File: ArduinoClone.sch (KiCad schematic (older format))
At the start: 0 parts

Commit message: added symboles and child sheet
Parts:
- added BT?: Battery, symbol Device:Battery
- added C? (x2): C, symbol Device:C
- added C?: CP, symbol Device:CP
- added D?: LED, symbol Device:LED
- added R? (x2): R, symbol Device:R
- added U?: 24LC1025, symbol Memory_EEPROM:24LC1025
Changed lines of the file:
@@
 $Descr A4 11693 8268
 encoding utf-8
-Sheet 1 1
-Title "Arduino Clone"
+Sheet 1 2
+Title "Battery powered Arduino clone with clock and extended EEPROM"
 Date "2020-04-18"
 Rev "1"
@@
 Comment4 ""
 $EndDescr
+$Comp
+L Device:Battery BT?
+U 1 1 5E9ADC39
+P 5200 3250
+F 0 "BT?" H 5308 3296 50  0000 L CNN
+F 1 "Battery" H 5308 3205 50  0000 L CNN
+F 2 "" V 5200 3310 50  0001 C CNN
+F 3 "~" V 5200 3310 50  0001 C CNN
+	1    5200 3250
+	1    0    0    -1
+$EndComp
+$Comp
+L Device:C C?
+U 1 1 5E9AE1F8
+P 5900 3150
+F 0 "C?" H 6015 3196 50  0000 L CNN
+F 1 "C" H 6015 3105 50  0000 L CNN
+F 2 "" H 5938 3000 50  0001 C CNN
+F 3 "~" H 5900 3150 50  0001 C CNN
+	1    5900 3150
+	1    0    0    -1
+$EndComp
+$Comp
+L Device:C C?
+U 1 1 5E9AE956
+P 5900 3600
+F 0 "C?" H 6015 3646 50  0000 L CNN
+F 1 "C" H 6015 3555 50  0000 L CNN
+F 2 "" H 5938 3450 50  0001 C CNN
+F 3 "~" H 5900 3600 50  0001 C CNN
+	1    5900 3600
+	1    0    0    -1
+$EndComp
+$Comp
+L Device:CP C?
+U 1 1 5E9AF047
+P 5900 4050
+F 0 "C?" H 6018 4096 50  0000 L CNN
+F 1 "CP" H 6018 4005 50  0000 L CNN
+F 2 "" H 5938 3900 50  0001 C CNN
+F 3 "~" H 5900 4050 50  0001 C CNN
+	1    5900 4050
+	1    0    0    -1
+$EndComp
+$Comp
+L Device:LED D?
+U 1 1 5E9AF4DB
+P 5200 3800
+F 0 "D?" H 5193 4016 50  0000 C CNN
+F 1 "LED" H 5193 3925 50  0000 C CNN
+F 2 "" H 5200 3800 50  0001 C CNN
+F 3 "~" H 5200 3800 50  0001 C CNN
+	1    5200 3800
+	1    0    0    -1
+$EndComp
+$Comp
+L Device:R R?
+U 1 1 5E9AF9BC
+P 6450 3750
+F 0 "R?" H 6520 3796 50  0000 L CNN
+F 1 "R" H 6520 3705 50  0000 L CNN
+F 2 "" V 6380 3750 50  0001 C CNN
+F 3 "~" H 6450 3750 50  0001 C CNN
+	1    6450 3750
+	1    0    0    -1
+$EndComp
+$Comp
+L Device:R R?
+U 1 1 5E9AFB62
+P 6450 3150
+F 0 "R?" H 6520 3196 50  0000 L CNN
+F 1 "R" H 6520 3105 50  0000 L CNN
+F 2 "" V 6380 3150 50  0001 C CNN
+F 3 "~" H 6450 3150 50  0001 C CNN
+	1    6450 3150
+	1    0    0    -1
+$EndComp
+$Comp
+L Memory_EEPROM:24LC1025 U?
+U 1 1 5E9B03F6
+P 7550 3100
+F 0 "U?" H 7550 3581 50  0000 C CNN
+F 1 "24LC1025" H 7550 3490 50  0000 C CNN
+F 2 "" H 7550 3100 50  0001 C CNN
+F 3 "http://ww1.microchip.com/downloads/en/DeviceDoc/21941B.pdf" H 7550 3100 50  0001 C CNN
+	1    7550 3100
+	1    0    0    -1
+$EndComp
+$Sheet
+S 7150 3800 1450 1850
+U 5E9B2945
+F0 "Connectors" 50
+F1 "connectors.sch" 50
+$EndSheet
 $EndSCHEMATC

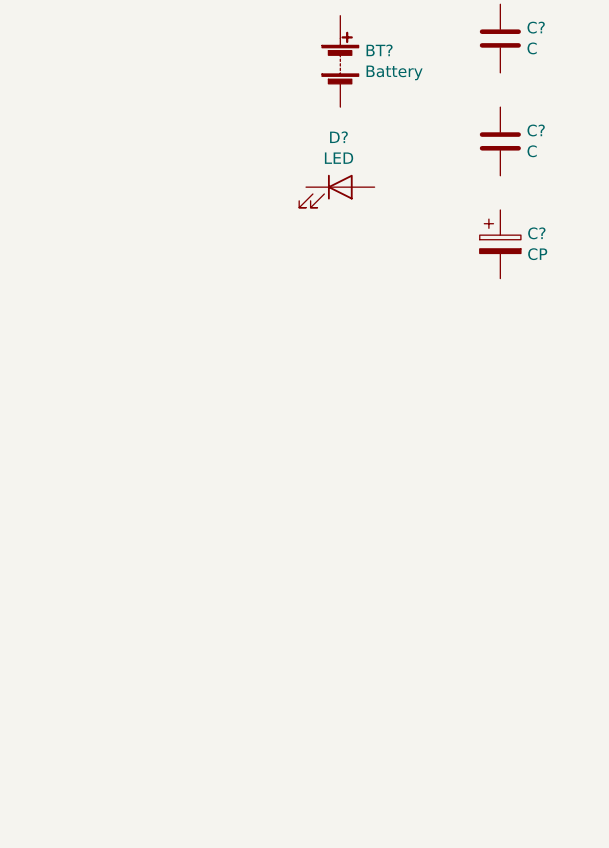
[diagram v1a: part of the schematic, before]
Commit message: added new symbol for Atmega328
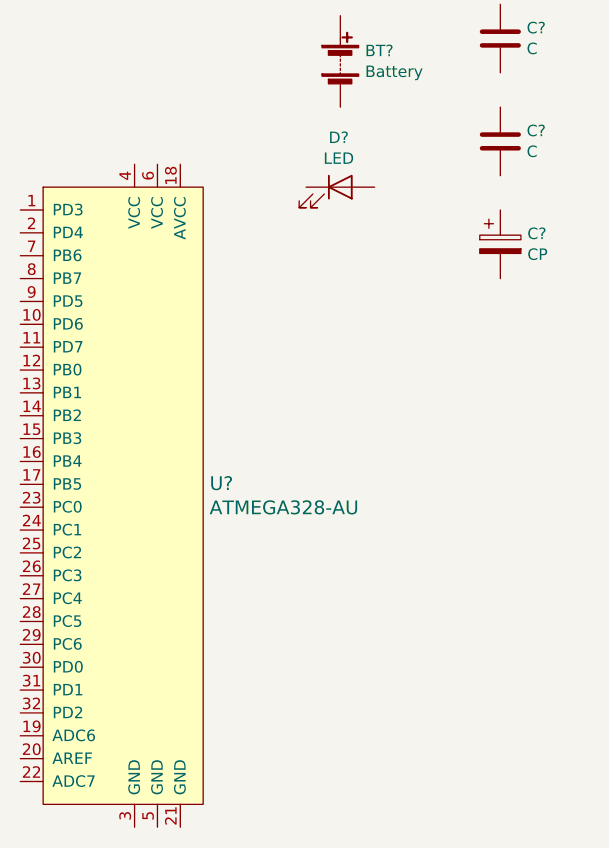
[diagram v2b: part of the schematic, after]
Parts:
- added U?: ATMEGA328-AU, digikey-footprints:TQFP-32_7x7mm, symbol dk_Embedded-Microcontrollers:ATMEGA328-AU
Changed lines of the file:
@@
 F1 "connectors.sch" 50
 $EndSheet
+$Comp
+L dk_Embedded-Microcontrollers:ATMEGA328-AU U?
+U 1 1 5E9B5F93
+P 4300 4300
+F 0 "U?" H 4628 3503 60  0000 L CNN
+F 1 "ATMEGA328-AU" H 4628 3397 60  0000 L CNN
+F 2 "digikey-footprints:TQFP-32_7x7mm" H 4500 4500 60  0001 L CNN
+F 3 "http://www.microchip.com/mymicrochip/filehandler.aspx?ddocname=en608326" H 4500 4600 60  0001 L CNN
+F 4 "ATMEGA328-AU-ND" H 4500 4700 60  0001 L CNN "Digi-Key_PN"
+F 5 "ATMEGA328-AU" H 4500 4800 60  0001 L CNN "MPN"
+F 6 "Integrated Circuits (ICs)" H 4500 4900 60  0001 L CNN "Category"
+F 7 "Embedded - Microcontrollers" H 4500 5000 60  0001 L CNN "Family"
+F 8 "http://www.microchip.com/mymicrochip/filehandler.aspx?ddocname=en608326" H 4500 5100 60  0001 L CNN "DK_Datasheet_Link"
+F 9 "/product-detail/en/microchip-technology/ATMEGA328-AU/ATMEGA328-AU-ND/2271029" H 4500 5200 60  0001 L CNN "DK_Detail_Page"
+F 10 "IC MCU 8BIT 32KB FLASH 32TQFP" H 4500 5300 60  0001 L CNN "Description"
+F 11 "Microchip Technology" H 4500 5400 60  0001 L CNN "Manufacturer"
+F 12 "Active" H 4500 5500 60  0001 L CNN "Status"
+	1    4300 4300
+	1    0    0    -1
+$EndComp
 $EndSCHEMATC

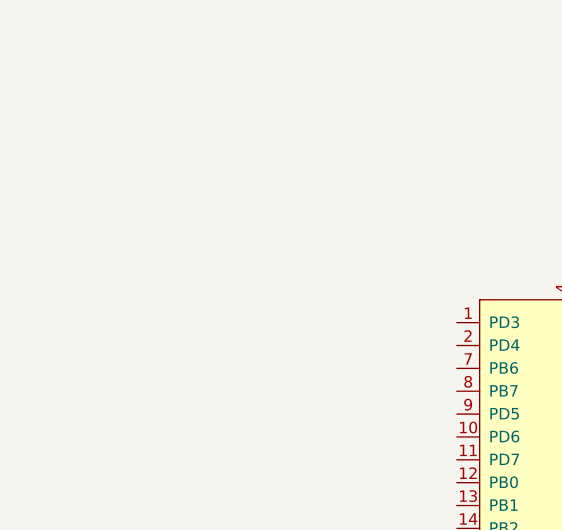
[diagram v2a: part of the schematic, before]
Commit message: created custom Symbol and added it
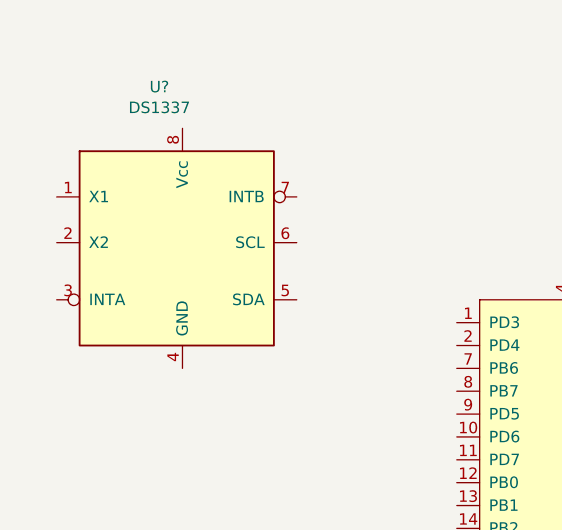
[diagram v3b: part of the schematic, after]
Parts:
- added U?: DS1337, symbol My_Library:DS1337
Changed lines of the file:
@@
+	1    0    0    -1
+$EndComp
+$Comp
+L My_Library:DS1337 U?
+U 1 1 5E9BB10B
+P 2600 3550
+F 0 "U?" H 2499 4231 50  0000 C CNN
+F 1 "DS1337" H 2499 4140 50  0000 C CNN
+F 2 "" H 2500 3950 50  0001 C CNN
+F 3 "" H 2500 3950 50  0001 C CNN
+	1    2600 3550
 	1    0    0    -1
 $EndComp

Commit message: Arranged symbols
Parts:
- added U?: 24LC1025, symbol Memory_EEPROM:24LC1025
- added Y? (x2): Crystal, symbol Device:Crystal
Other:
- moved on the sheet: BT?, C?, D?, R?, U?
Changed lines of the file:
@@
 L Device:Battery BT?
 U 1 1 5E9ADC39
-P 5200 3250
-F 0 "BT?" H 5308 3296 50  0000 L CNN
-F 1 "Battery" H 5308 3205 50  0000 L CNN
-F 2 "" V 5200 3310 50  0001 C CNN
-F 3 "~" V 5200 3310 50  0001 C CNN
-	1    5200 3250
+P 9650 2200
+F 0 "BT?" H 9758 2246 50  0000 L CNN
+F 1 "Battery" H 9758 2155 50  0000 L CNN
+F 2 "" V 9650 2260 50  0001 C CNN
+F 3 "~" V 9650 2260 50  0001 C CNN
+	1    9650 2200
 	1    0    0    -1
 $EndComp
@@
 L Device:C C?
 U 1 1 5E9AE1F8
-P 5900 3150
-F 0 "C?" H 6015 3196 50  0000 L CNN
-F 1 "C" H 6015 3105 50  0000 L CNN
-F 2 "" H 5938 3000 50  0001 C CNN
-F 3 "~" H 5900 3150 50  0001 C CNN
-	1    5900 3150
+P 5550 2250
+F 0 "C?" H 5665 2296 50  0000 L CNN
+F 1 "C" H 5665 2205 50  0000 L CNN
+F 2 "" H 5588 2100 50  0001 C CNN
+F 3 "~" H 5550 2250 50  0001 C CNN
+	1    5550 2250
 	1    0    0    -1
 $EndComp
@@
 L Device:C C?
 U 1 1 5E9AE956
-P 5900 3600
-F 0 "C?" H 6015 3646 50  0000 L CNN
-F 1 "C" H 6015 3555 50  0000 L CNN
-F 2 "" H 5938 3450 50  0001 C CNN
-F 3 "~" H 5900 3600 50  0001 C CNN
-	1    5900 3600
+P 5550 2750
+F 0 "C?" H 5665 2796 50  0000 L CNN
+F 1 "C" H 5665 2705 50  0000 L CNN
+F 2 "" H 5588 2600 50  0001 C CNN
+F 3 "~" H 5550 2750 50  0001 C CNN
+	1    5550 2750
 	1    0    0    -1
 $EndComp
@@
 L Device:CP C?
 U 1 1 5E9AF047
-P 5900 4050
-F 0 "C?" H 6018 4096 50  0000 L CNN
-F 1 "CP" H 6018 4005 50  0000 L CNN
-F 2 "" H 5938 3900 50  0001 C CNN
-F 3 "~" H 5900 4050 50  0001 C CNN
-	1    5900 4050
+P 9650 2800
+F 0 "C?" H 9768 2846 50  0000 L CNN
+F 1 "CP" H 9768 2755 50  0000 L CNN
+F 2 "" H 9688 2650 50  0001 C CNN
+F 3 "~" H 9650 2800 50  0001 C CNN
+	1    9650 2800
 	1    0    0    -1
 $EndComp
@@
 L Device:LED D?
 U 1 1 5E9AF4DB
-P 5200 3800
-F 0 "D?" H 5193 4016 50  0000 C CNN
-F 1 "LED" H 5193 3925 50  0000 C CNN
-F 2 "" H 5200 3800 50  0001 C CNN
-F 3 "~" H 5200 3800 50  0001 C CNN
-	1    5200 3800
+P 6350 3500
+F 0 "D?" H 6343 3716 50  0000 C CNN
+F 1 "LED" H 6343 3625 50  0000 C CNN
+F 2 "" H 6350 3500 50  0001 C CNN
+F 3 "~" H 6350 3500 50  0001 C CNN
+	1    6350 3500
 	1    0    0    -1
 $EndComp
@@
 L Device:R R?
 U 1 1 5E9AF9BC
-P 6450 3750
-F 0 "R?" H 6520 3796 50  0000 L CNN
-F 1 "R" H 6520 3705 50  0000 L CNN
-F 2 "" V 6380 3750 50  0001 C CNN
-F 3 "~" H 6450 3750 50  0001 C CNN
-	1    6450 3750
+P 5950 4350
+F 0 "R?" H 6020 4396 50  0000 L CNN
+F 1 "R" H 6020 4305 50  0000 L CNN
+F 2 "" V 5880 4350 50  0001 C CNN
+F 3 "~" H 5950 4350 50  0001 C CNN
+	1    5950 4350
 	1    0    0    -1
 $EndComp
@@
 L Device:R R?
 U 1 1 5E9AFB62
-P 6450 3150
-F 0 "R?" H 6520 3196 50  0000 L CNN
-F 1 "R" H 6520 3105 50  0000 L CNN
-F 2 "" V 6380 3150 50  0001 C CNN
-F 3 "~" H 6450 3150 50  0001 C CNN
-	1    6450 3150
+P 5500 3500
+F 0 "R?" H 5570 3546 50  0000 L CNN
+F 1 "R" H 5570 3455 50  0000 L CNN
+F 2 "" V 5430 3500 50  0001 C CNN
+F 3 "~" H 5500 3500 50  0001 C CNN
+	1    5500 3500
 	1    0    0    -1
 $EndComp
@@
 L Memory_EEPROM:24LC1025 U?
 U 1 1 5E9B03F6
-P 7550 3100
-F 0 "U?" H 7550 3581 50  0000 C CNN
-F 1 "24LC1025" H 7550 3490 50  0000 C CNN
-F 2 "" H 7550 3100 50  0001 C CNN
-F 3 "http://ww1.microchip.com/downloads/en/DeviceDoc/21941B.pdf" H 7550 3100 50  0001 C CNN
-	1    7550 3100
+P 2000 4100
+F 0 "U?" H 2000 4581 50  0000 C CNN
+F 1 "24LC1025" H 2000 4490 50  0000 C CNN
+F 2 "" H 2000 4100 50  0001 C CNN
+F 3 "http://ww1.microchip.com/downloads/en/DeviceDoc/21941B.pdf" H 2000 4100 50  0001 C CNN
+	1    2000 4100
 	1    0    0    -1
 $EndComp
 $Sheet
-S 7150 3800 1450 1850
+S 8950 4050 1450 1850
 U 5E9B2945
 F0 "Connectors" 50
@@
 L dk_Embedded-Microcontrollers:ATMEGA328-AU U?
 U 1 1 5E9B5F93
-P 4300 4300
-F 0 "U?" H 4628 3503 60  0000 L CNN
-F 1 "ATMEGA328-AU" H 4628 3397 60  0000 L CNN
-F 2 "digikey-footprints:TQFP-32_7x7mm" H 4500 4500 60  0001 L CNN
-F 3 "http://www.microchip.com/mymicrochip/filehandler.aspx?ddocname=en608326" H 4500 4600 60  0001 L CNN
-F 4 "ATMEGA328-AU-ND" H 4500 4700 60  0001 L CNN "Digi-Key_PN"
-F 5 "ATMEGA328-AU" H 4500 4800 60  0001 L CNN "MPN"
-F 6 "Integrated Circuits (ICs)" H 4500 4900 60  0001 L CNN "Category"
-F 7 "Embedded - Microcontrollers" H 4500 5000 60  0001 L CNN "Family"
-F 8 "http://www.microchip.com/mymicrochip/filehandler.aspx?ddocname=en608326" H 4500 5100 60  0001 L CNN "DK_Datasheet_Link"
-F 9 "/product-detail/en/microchip-technology/ATMEGA328-AU/ATMEGA328-AU-ND/2271029" H 4500 5200 60  0001 L CNN "DK_Detail_Page"
-F 10 "IC MCU 8BIT 32KB FLASH 32TQFP" H 4500 5300 60  0001 L CNN "Description"
-F 11 "Microchip Technology" H 4500 5400 60  0001 L CNN "Manufacturer"
-F 12 "Active" H 4500 5500 60  0001 L CNN "Status"
-	1    4300 4300
+P 7450 2450
+F 0 "U?" H 7778 1653 60  0000 L CNN
+F 1 "ATMEGA328-AU" H 7778 1547 60  0000 L CNN
+F 2 "digikey-footprints:TQFP-32_7x7mm" H 7650 2650 60  0001 L CNN
+F 3 "http://www.microchip.com/mymicrochip/filehandler.aspx?ddocname=en608326" H 7650 2750 60  0001 L CNN
+F 4 "ATMEGA328-AU-ND" H 7650 2850 60  0001 L CNN "Digi-Key_PN"
+F 5 "ATMEGA328-AU" H 7650 2950 60  0001 L CNN "MPN"
+F 6 "Integrated Circuits (ICs)" H 7650 3050 60  0001 L CNN "Category"
+F 7 "Embedded - Microcontrollers" H 7650 3150 60  0001 L CNN "Family"
+F 8 "http://www.microchip.com/mymicrochip/filehandler.aspx?ddocname=en608326" H 7650 3250 60  0001 L CNN "DK_Datasheet_Link"
+F 9 "/product-detail/en/microchip-technology/ATMEGA328-AU/ATMEGA328-AU-ND/2271029" H 7650 3350 60  0001 L CNN "DK_Detail_Page"
+F 10 "IC MCU 8BIT 32KB FLASH 32TQFP" H 7650 3450 60  0001 L CNN "Description"
+F 11 "Microchip Technology" H 7650 3550 60  0001 L CNN "Manufacturer"
+F 12 "Active" H 7650 3650 60  0001 L CNN "Status"
+	1    7450 2450
 	1    0    0    -1
 $EndComp
@@
 L My_Library:DS1337 U?
 U 1 1 5E9BB10B
-P 2600 3550
-F 0 "U?" H 2499 4231 50  0000 C CNN
-F 1 "DS1337" H 2499 4140 50  0000 C CNN
-F 2 "" H 2500 3950 50  0001 C CNN
-F 3 "" H 2500 3950 50  0001 C CNN
-	1    2600 3550
+P 2000 2550
+F 0 "U?" H 1899 3231 50  0000 C CNN
+F 1 "DS1337" H 1899 3140 50  0000 C CNN
+F 2 "" H 1900 2950 50  0001 C CNN
+F 3 "" H 1900 2950 50  0001 C CNN
+	1    2000 2550
 	1    0    0    -1
 $EndComp
+$Comp
+L Device:Crystal Y?
+U 1 1 5E9BBC39
+P 6200 2250
+F 0 "Y?" V 6154 2381 50  0000 L CNN
+F 1 "Crystal" V 6245 2381 50  0000 L CNN
+F 2 "" H 6200 2250 50  0001 C CNN
+F 3 "~" H 6200 2250 50  0001 C CNN
+	1    6200 2250
+	0    1    1    0
+$EndComp
+$Comp
+L Device:Crystal Y?
+U 1 1 5E9BC818
+P 1150 2350
+F 0 "Y?" H 1150 2618 50  0000 C CNN
+F 1 "Crystal" H 1150 2527 50  0000 C CNN
+F 2 "" H 1150 2350 50  0001 C CNN
+F 3 "~" H 1150 2350 50  0001 C CNN
+	1    1150 2350
+	1    0    0    -1
+$EndComp
+$Comp
+L Memory_EEPROM:24LC1025 U?
+U 1 1 5E9BFEC6
+P 2000 5200
+F 0 "U?" H 2000 5681 50  0000 C CNN
+F 1 "24LC1025" H 2000 5590 50  0000 C CNN
+F 2 "" H 2000 5200 50  0001 C CNN
+F 3 "http://ww1.microchip.com/downloads/en/DeviceDoc/21941B.pdf" H 2000 5200 50  0001 C CNN
+	1    2000 5200
+	1    0    0    -1
+$EndComp
+$Comp
+L power:GND #PWR?
+U 1 1 5E9CDC4A
+P 9650 3600
+F 0 "#PWR?" H 9650 3350 50  0001 C CNN
+F 1 "GND" H 9655 3427 50  0000 C CNN
+F 2 "" H 9650 3600 50  0001 C CNN
+F 3 "" H 9650 3600 50  0001 C CNN
+	1    9650 3600
+	1    0    0    -1
+$EndComp

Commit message: Annotated
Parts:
- gave numbers to parts that had none: 13
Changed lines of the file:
@@
 $EndDescr
 $Comp
-L Device:Battery BT?
+L Device:Battery BT1
 U 1 1 5E9ADC39
 P 9650 2200
-F 0 "BT?" H 9758 2246 50  0000 L CNN
+F 0 "BT1" H 9758 2246 50  0000 L CNN
 F 1 "Battery" H 9758 2155 50  0000 L CNN
 F 2 "" V 9650 2260 50  0001 C CNN
@@
 $EndComp
 $Comp
-L Device:C C?
+L Device:C C1
 U 1 1 5E9AE1F8
 P 5550 2250
-F 0 "C?" H 5665 2296 50  0000 L CNN
+F 0 "C1" H 5665 2296 50  0000 L CNN
 F 1 "C" H 5665 2205 50  0000 L CNN
 F 2 "" H 5588 2100 50  0001 C CNN
@@
 $EndComp
 $Comp
-L Device:C C?
+L Device:C C2
 U 1 1 5E9AE956
 P 5550 2750
-F 0 "C?" H 5665 2796 50  0000 L CNN
+F 0 "C2" H 5665 2796 50  0000 L CNN
 F 1 "C" H 5665 2705 50  0000 L CNN
 F 2 "" H 5588 2600 50  0001 C CNN
@@
 $EndComp
 $Comp
-L Device:CP C?
+L Device:CP C3
 U 1 1 5E9AF047
 P 9650 2800
-F 0 "C?" H 9768 2846 50  0000 L CNN
+F 0 "C3" H 9768 2846 50  0000 L CNN
 F 1 "CP" H 9768 2755 50  0000 L CNN
 F 2 "" H 9688 2650 50  0001 C CNN
@@
 $EndComp
 $Comp
-L Device:LED D?
+L Device:LED D1
 U 1 1 5E9AF4DB
 P 6350 3500
-F 0 "D?" H 6343 3716 50  0000 C CNN
+F 0 "D1" H 6343 3716 50  0000 C CNN
 F 1 "LED" H 6343 3625 50  0000 C CNN
 F 2 "" H 6350 3500 50  0001 C CNN
@@
 $EndComp
 $Comp
-L Device:R R?
+L Device:R R2
 U 1 1 5E9AF9BC
 P 5950 4350
-F 0 "R?" H 6020 4396 50  0000 L CNN
+F 0 "R2" H 6020 4396 50  0000 L CNN
 F 1 "R" H 6020 4305 50  0000 L CNN
 F 2 "" V 5880 4350 50  0001 C CNN
@@
 $EndComp
 $Comp
-L Device:R R?
+L Device:R R1
 U 1 1 5E9AFB62
 P 5500 3500
-F 0 "R?" H 5570 3546 50  0000 L CNN
+F 0 "R1" H 5570 3546 50  0000 L CNN
 F 1 "R" H 5570 3455 50  0000 L CNN
 F 2 "" V 5430 3500 50  0001 C CNN
@@
 $EndComp
 $Comp
-L Memory_EEPROM:24LC1025 U?
+L Memory_EEPROM:24LC1025 U2
 U 1 1 5E9B03F6
 P 2000 4100
-F 0 "U?" H 2000 4581 50  0000 C CNN
+F 0 "U2" H 2000 4581 50  0000 C CNN
 F 1 "24LC1025" H 2000 4490 50  0000 C CNN
 F 2 "" H 2000 4100 50  0001 C CNN
@@
 $EndSheet
 $Comp
-L dk_Embedded-Microcontrollers:ATMEGA328-AU U?
+L dk_Embedded-Microcontrollers:ATMEGA328-AU U4
 U 1 1 5E9B5F93
 P 7450 2450
-F 0 "U?" H 7778 1653 60  0000 L CNN
+F 0 "U4" H 7778 1653 60  0000 L CNN
 F 1 "ATMEGA328-AU" H 7778 1547 60  0000 L CNN
 F 2 "digikey-footprints:TQFP-32_7x7mm" H 7650 2650 60  0001 L CNN
@@
 $EndComp
 $Comp
-L My_Library:DS1337 U?
+L My_Library:DS1337 U1
 U 1 1 5E9BB10B
 P 2000 2550
-F 0 "U?" H 1899 3231 50  0000 C CNN
+F 0 "U1" H 1899 3231 50  0000 C CNN
 F 1 "DS1337" H 1899 3140 50  0000 C CNN
 F 2 "" H 1900 2950 50  0001 C CNN
@@
 $EndComp
 $Comp
-L Device:Crystal Y?
+L Device:Crystal Y2
 U 1 1 5E9BBC39
 P 6200 2250
-F 0 "Y?" V 6154 2381 50  0000 L CNN
+F 0 "Y2" V 6154 2381 50  0000 L CNN
 F 1 "Crystal" V 6245 2381 50  0000 L CNN
 F 2 "" H 6200 2250 50  0001 C CNN
@@
 $EndComp
 $Comp
-L Device:Crystal Y?
+L Device:Crystal Y1
 U 1 1 5E9BC818
 P 1150 2350
-F 0 "Y?" H 1150 2618 50  0000 C CNN
+F 0 "Y1" H 1150 2618 50  0000 C CNN
 F 1 "Crystal" H 1150 2527 50  0000 C CNN
 F 2 "" H 1150 2350 50  0001 C CNN
@@
 $EndComp
 $Comp
-L Memory_EEPROM:24LC1025 U?
+L Memory_EEPROM:24LC1025 U3
 U 1 1 5E9BFEC6
 P 2000 5200
-F 0 "U?" H 2000 5681 50  0000 C CNN
+F 0 "U3" H 2000 5681 50  0000 C CNN
 F 1 "24LC1025" H 2000 5590 50  0000 C CNN
 F 2 "" H 2000 5200 50  0001 C CNN
@@
 $EndComp
 $Comp
-L power:GND #PWR?
+L power:GND #PWR01
 U 1 1 5E9CDC4A
 P 9650 3600
-F 0 "#PWR?" H 9650 3350 50  0001 C CNN
+F 0 "#PWR01" H 9650 3350 50  0001 C CNN
 F 1 "GND" H 9655 3427 50  0000 C CNN
 F 2 "" H 9650 3600 50  0001 C CNN
